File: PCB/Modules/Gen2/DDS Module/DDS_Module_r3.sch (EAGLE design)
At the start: 36 parts, among them IC1 SN65HVD31DR, IC2 LM3480-5.0, IC3 AD9834, IC4 SN65HVD31DR, IC5 AD5620BRJZ-2500RL7, J1 BNCPTH, Y1 ASE10MHZ

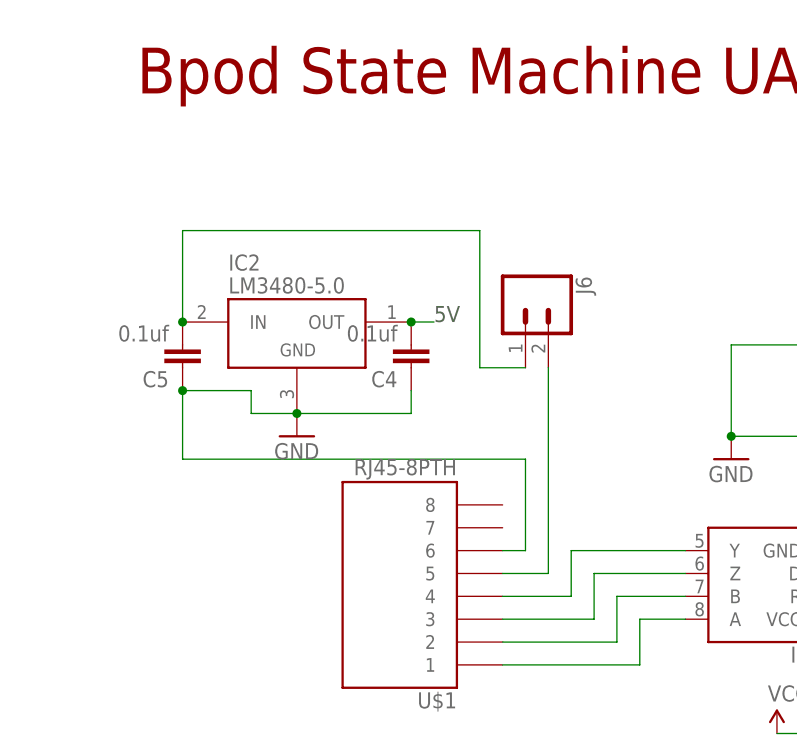
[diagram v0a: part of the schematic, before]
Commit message: -Critical Update for modules with optional RJ45 power (ValveDriver, I2C, SNES and DDS); new PCB designs add a diode to prevent USB power from entering output pin of 5V regulator, when RJ45 (state machine) power is not connected. This update greatly reduces unnecessary power consumption and heat dissipation. If you built a board using the previous designs, please Email a photo of your board to Sanworks support for a free upgrade. -Updated component names on some boards and on web BOMs to avoid skipping parts -Renamed Gen2 module PCB folder from '0.7' to 'Gen2' -Retired pocket state machine (to be replaced with Bpod State Machine r1)
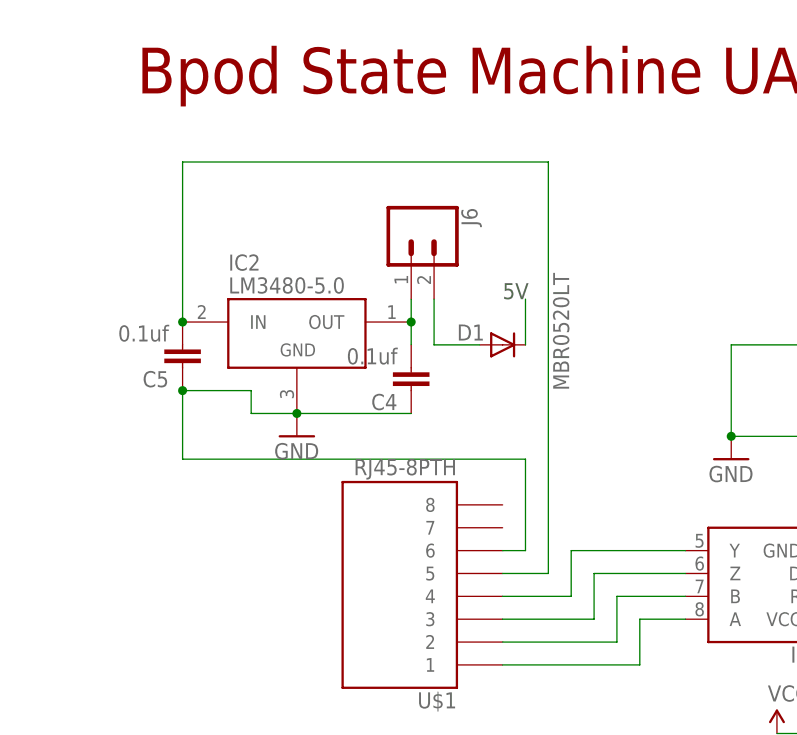
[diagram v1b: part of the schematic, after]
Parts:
- added D1: MBR0520LT, diode:MBR0520LT
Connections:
- removed net N$26: C5.2, IC2.IN, J6.1
- new net N$14: C4.2, IC2.OUT, J6.1
- new net N$18: D1.A, J6.2
- net 5V: now also D1.C; no longer C4.2, IC2.OUT
- net N$24: now also C5.2, IC2.IN; no longer J6.2
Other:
- moved on the sheet: C4, J6
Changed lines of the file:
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@@
 <part name="C3" library="SparkFun-Capacitors" deviceset="10UF" device="-0805-10V-10%" value="0.01uF"/>
 <part name="GND16" library="SparkFun-Aesthetics" deviceset="GND" device=""/>
+<part name="D1" library="diode" deviceset="MBR0520LT" device=""/>
 </parts>
 <sheets>
@@
 <plain>
 <text x="165.1" y="40.64" size="1.778" layer="97">5V</text>
-<text x="-83.82" y="198.12" size="1.778" layer="97">5V</text>
+<text x="-76.2" y="200.66" size="1.778" layer="97">5V</text>
 <text x="-25.4" y="50.8" size="1.778" layer="91">RX2</text>
 <text x="-25.4" y="53.34" size="1.778" layer="91">TX2</text>
@@
 <instance part="H3" gate="G$1" x="78.74" y="-7.62"/>
 <instance part="H4" gate="G$1" x="104.14" y="-7.62"/>
-<instance part="J6" gate="G$1" x="-73.66" y="200.66" rot="R270"/>
+<instance part="J6" gate="G$1" x="-86.36" y="208.28" rot="R270"/>
 <instance part="IC2" gate="G$1" x="-99.06" y="198.12"/>
-<instance part="C4" gate="G$1" x="-86.36" y="195.58" rot="R180"/>
+<instance part="C4" gate="G$1" x="-86.36" y="193.04" rot="R180"/>
 <instance part="C5" gate="G$1" x="-111.76" y="195.58" rot="R180"/>
 <instance part="GND5" gate="1" x="-99.06" y="185.42"/>
@@
 <instance part="C3" gate="G$1" x="144.78" y="114.3" rot="R180"/>
 <instance part="GND16" gate="1" x="144.78" y="104.14"/>
+<instance part="D1" gate="G$1" x="-76.2" y="195.58" smashed="yes">
+<attribute name="NAME" x="-81.28" y="196.0626" size="1.778" layer="95"/>
+<attribute name="VALUE" x="-68.8086" y="190.5" size="1.778" layer="96" rot="R90"/>
+</instance>
 </instances>
 <busses>
@@
 <pinref part="C4" gate="G$1" pin="1"/>
 <wire x1="-99.06" y1="187.96" x2="-86.36" y2="187.96" width="0.1524" layer="91"/>
-<wire x1="-86.36" y1="187.96" x2="-86.36" y2="190.5" width="0.1524" layer="91"/>
 <junction x="-99.06" y="187.96"/>
 <pinref part="GND5" gate="1" pin="GND"/>
@@
 </segment>
 <segment>
-<pinref part="IC2" gate="G$1" pin="OUT"/>
-<wire x1="-86.36" y1="198.12" x2="-83.82" y2="198.12" width="0.1524" layer="91"/>
-<pinref part="C4" gate="G$1" pin="2"/>
-<junction x="-86.36" y="198.12"/>
+<pinref part="D1" gate="G$1" pin="C"/>
+<wire x1="-73.66" y1="195.58" x2="-73.66" y2="200.66" width="0.1524" layer="91"/>
 </segment>
 </net>
@@
 <segment>
 <pinref part="U$1" gate="G$1" pin="5"/>
-<pinref part="J6" gate="G$1" pin="2"/>
 <wire x1="-76.2" y1="170.18" x2="-71.12" y2="170.18" width="0.1524" layer="91"/>
-<wire x1="-71.12" y1="170.18" x2="-71.12" y2="193.04" width="0.1524" layer="91"/>
-</segment>
-</net>
-<net name="N$26" class="0">
-<segment>
-<pinref part="J6" gate="G$1" pin="1"/>
-<wire x1="-73.66" y1="193.04" x2="-78.74" y2="193.04" width="0.1524" layer="91"/>
-<wire x1="-78.74" y1="193.04" x2="-78.74" y2="208.28" width="0.1524" layer="91"/>
+<wire x1="-71.12" y1="170.18" x2="-71.12" y2="215.9" width="0.1524" layer="91"/>
 <pinref part="IC2" gate="G$1" pin="IN"/>
-<wire x1="-78.74" y1="208.28" x2="-111.76" y2="208.28" width="0.1524" layer="91"/>
-<wire x1="-111.76" y1="208.28" x2="-111.76" y2="198.12" width="0.1524" layer="91"/>
+<wire x1="-71.12" y1="215.9" x2="-111.76" y2="215.9" width="0.1524" layer="91"/>
+<wire x1="-111.76" y1="215.9" x2="-111.76" y2="198.12" width="0.1524" layer="91"/>
 <pinref part="C5" gate="G$1" pin="2"/>
 <junction x="-111.76" y="198.12"/>
@@
 </segment>
 </net>
+<net name="N$14" class="0">
+<segment>
+<pinref part="IC2" gate="G$1" pin="OUT"/>
+<pinref part="C4" gate="G$1" pin="2"/>
+<wire x1="-86.36" y1="198.12" x2="-86.36" y2="195.58" width="0.1524" layer="91"/>
+<pinref part="J6" gate="G$1" pin="1"/>
+<wire x1="-86.36" y1="198.12" x2="-86.36" y2="200.66" width="0.1524" layer="91"/>
+<junction x="-86.36" y="198.12"/>
+</segment>
+</net>
+<net name="N$18" class="0">
+<segment>
+<pinref part="J6" gate="G$1" pin="2"/>
+<wire x1="-83.82" y1="200.66" x2="-83.82" y2="195.58" width="0.1524" layer="91"/>
+<pinref part="D1" gate="G$1" pin="A"/>
+<wire x1="-83.82" y1="195.58" x2="-78.74" y2="195.58" width="0.1524" layer="91"/>
+</segment>
+</net>
